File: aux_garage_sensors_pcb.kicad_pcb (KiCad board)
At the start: 2 copper layers, 48 x 38 mm, 22 parts, among them J1 PJ-102AH, J2 TBL003-254-06GR-2OR, Q1 IRLML0040TRPBF, Q2 IRLML0040TRPBF, U1 CD14538B

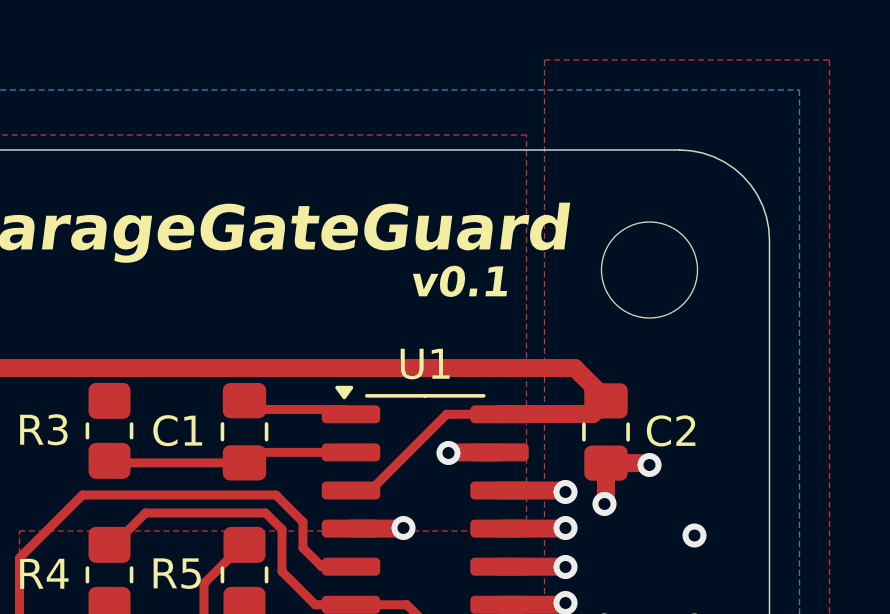
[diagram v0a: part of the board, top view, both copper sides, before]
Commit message: added date and git info to silkscreen
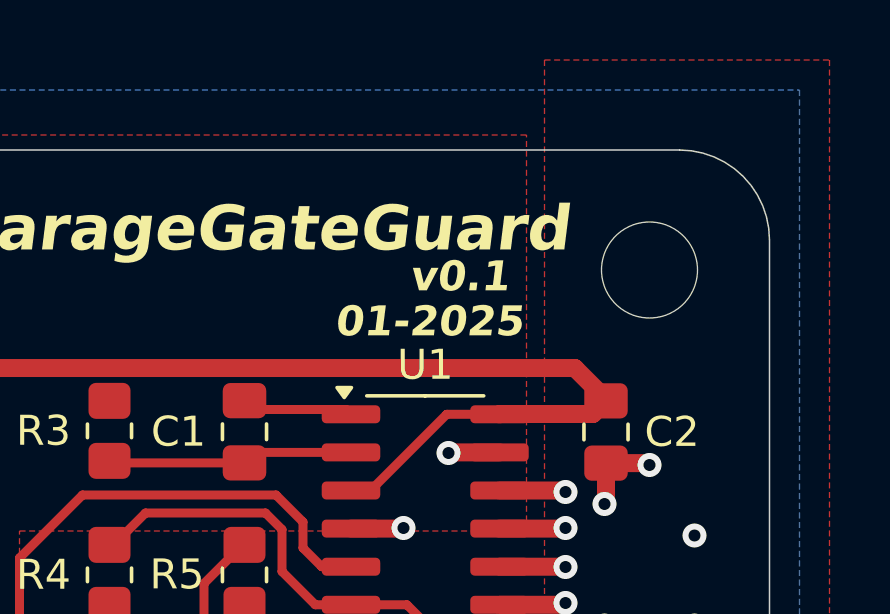
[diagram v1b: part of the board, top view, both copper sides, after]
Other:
- board text added: "01-2025"
- board text added: "github.com/wynn4/aux_garage_sensors_pcb"

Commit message: added BOM and v0.1 manufacturing files
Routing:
- net 6VDC: track 42.6 -> 43.5 mm
- net GND: vias 41 -> 40
